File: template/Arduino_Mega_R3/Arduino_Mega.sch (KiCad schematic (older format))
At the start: 7 parts, among them P1 Digital, P2 Power, P3 Analog, P4 Analog, P5 PWM, P6 PWM, P7 Communication

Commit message: correction holes
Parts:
- added P10, P11, P12, P13, P8, P9: CONN_1, Connect:1pin, symbol CONN_1
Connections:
- no-connect marks 1 -> 7
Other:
- note added: "Holes"
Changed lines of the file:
@@
 Wire Notes Line
 	7900 6300 7900 475
+$Comp
+L CONN_1 P8
+U 1 1 551BBA20
+P 8050 650
+F 0 "P8" H 8130 650 40  0000 L CNN
+F 1 "CONN_1" H 8050 705 30  0001 C CNN
+F 2 "Connect:1pin" H 8050 650 60  0001 C CNN
+F 3 "" H 8050 650 60  0000 C CNN
+	1    8050 650
+	0    -1   -1   0
+$EndComp
+$Comp
+L CONN_1 P9
+U 1 1 551BBB85
+P 8125 650
+F 0 "P9" H 8205 650 40  0000 L CNN
+F 1 "CONN_1" H 8125 705 30  0001 C CNN
+F 2 "Connect:1pin" H 8125 650 60  0001 C CNN
+F 3 "" H 8125 650 60  0000 C CNN
+	1    8125 650
+	0    -1   -1   0
+$EndComp
+$Comp
+L CONN_1 P10
+U 1 1 551BBBAB
+P 8200 650
+F 0 "P10" H 8280 650 40  0000 L CNN
+F 1 "CONN_1" H 8200 705 30  0001 C CNN
+F 2 "Connect:1pin" H 8200 650 60  0001 C CNN
+F 3 "" H 8200 650 60  0000 C CNN
+	1    8200 650
+	0    -1   -1   0
+$EndComp
+$Comp
+L CONN_1 P11
+U 1 1 551BBBD7
+P 8275 650
+F 0 "P11" H 8355 650 40  0000 L CNN
+F 1 "CONN_1" H 8275 705 30  0001 C CNN
+F 2 "Connect:1pin" H 8275 650 60  0001 C CNN
+F 3 "" H 8275 650 60  0000 C CNN
+	1    8275 650
+	0    -1   -1   0
+$EndComp
+$Comp
+L CONN_1 P12
+U 1 1 551BBC10
+P 8350 650
+F 0 "P12" H 8430 650 40  0000 L CNN
+F 1 "CONN_1" H 8350 705 30  0001 C CNN
+F 2 "Connect:1pin" H 8350 650 60  0001 C CNN
+F 3 "" H 8350 650 60  0000 C CNN
+	1    8350 650
+	0    -1   -1   0
+$EndComp
+$Comp
+L CONN_1 P13
+U 1 1 551BBC3C
+P 8425 650
+F 0 "P13" H 8505 650 40  0000 L CNN
+F 1 "CONN_1" H 8425 705 30  0001 C CNN
+F 2 "Connect:1pin" H 8425 650 60  0001 C CNN
+F 3 "" H 8425 650 60  0000 C CNN
+	1    8425 650
+	0    -1   -1   0
+$EndComp
+NoConn ~ 8050 800
+NoConn ~ 8125 800
+NoConn ~ 8200 800
+NoConn ~ 8275 800
+NoConn ~ 8350 800
+NoConn ~ 8425 800
+Text Notes 8125 925  0    60   ~ 0
+Holes
+Wire Notes Line
+	7900 950  8575 950
+Wire Notes Line
+	8575 950  8575 475
 $EndSCHEMATC

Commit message: Correction schématics
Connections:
- net labels added: 0(Rx0), 1(Tx0), 14(Tx3), 15(Rx3), 16(Tx2), 17(Rx2), 18(Tx1), 19(Rx1)
- net labels removed: 0(Rx), 1(Tx), 14(Tx), 15(Rx), 16(Tx), 17(Rx), 18(Tx), 19(Rx)
- wire segments 96 -> 98
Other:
- moved on the sheet: P10, P11, P12, P13, P2, P3, P4, P5, P6, P7, P8, P9

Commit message: corrections
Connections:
- net labels removed: NC
- wire segments 98 -> 97
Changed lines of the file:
@@
 	-1   0    0    -1
 $EndComp
-NoConn ~ 8425 1425
-Text Label 8450 1425 0    60   ~ 0
-NC
+NoConn ~ 9200 1425
 Text Label 9125 1250 1    60   ~ 0
 IOREF
@@
 Connection ~ 9125 2025
 Wire Wire Line
-	9200 1425 8425 1425
-Wire Wire Line
 	9200 1625 8425 1625

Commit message: add footprint Uno and Mega
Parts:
- P10, P11, P12, P13, P8, P9: footprint Connect:1pin -> Socket_Arduino_Mega:Arduino_1pin
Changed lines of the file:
@@
 F 0 "P8" H 10805 700 40  0000 L CNN
 F 1 "CONN_1" H 10725 755 30  0001 C CNN
-F 2 "Connect:1pin" H 10725 700 60  0001 C CNN
+F 2 "Socket_Arduino_Mega:Arduino_1pin" H 10725 700 60  0001 C CNN
 F 3 "" H 10725 700 60  0000 C CNN
 	1    10725 700
@@
 F 0 "P9" H 10880 700 40  0000 L CNN
 F 1 "CONN_1" H 10800 755 30  0001 C CNN
-F 2 "Connect:1pin" H 10800 700 60  0001 C CNN
+F 2 "Socket_Arduino_Mega:Arduino_1pin" H 10800 700 60  0001 C CNN
 F 3 "" H 10800 700 60  0000 C CNN
 	1    10800 700
@@
 F 0 "P10" H 10955 700 40  0000 L CNN
 F 1 "CONN_1" H 10875 755 30  0001 C CNN
-F 2 "Connect:1pin" H 10875 700 60  0001 C CNN
+F 2 "Socket_Arduino_Mega:Arduino_1pin" H 10875 700 60  0001 C CNN
 F 3 "" H 10875 700 60  0000 C CNN
 	1    10875 700
@@
 F 0 "P11" H 11030 700 40  0000 L CNN
 F 1 "CONN_1" H 10950 755 30  0001 C CNN
-F 2 "Connect:1pin" H 10950 700 60  0001 C CNN
+F 2 "Socket_Arduino_Mega:Arduino_1pin" H 10950 700 60  0001 C CNN
 F 3 "" H 10950 700 60  0000 C CNN
 	1    10950 700
@@
 F 0 "P12" H 11105 700 40  0000 L CNN
 F 1 "CONN_1" H 11025 755 30  0001 C CNN
-F 2 "Connect:1pin" H 11025 700 60  0001 C CNN
+F 2 "Socket_Arduino_Mega:Arduino_1pin" H 11025 700 60  0001 C CNN
 F 3 "" H 11025 700 60  0000 C CNN
 	1    11025 700
@@
 F 0 "P13" H 11180 700 40  0000 L CNN
 F 1 "CONN_1" H 11100 755 30  0001 C CNN
-F 2 "Connect:1pin" H 11100 700 60  0001 C CNN
+F 2 "Socket_Arduino_Mega:Arduino_1pin" H 11100 700 60  0001 C CNN
 F 3 "" H 11100 700 60  0000 C CNN
 	1    11100 700

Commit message: rebuilt shematic and fix librairie
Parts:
- removed P1: Digital, Socket_Arduino_Mega:Socket_Strip_Arduino_2x18, symbol CONN_18X2
- removed P10, P11, P12, P13, P8, P9: CONN_1, Socket_Arduino_Mega:Arduino_1pin, symbol CONN_1
- removed P2: Power, Socket_Arduino_Mega:Socket_Strip_Arduino_1x08, symbol CONN_8
- removed P3, P4: Analog, Socket_Arduino_Mega:Socket_Strip_Arduino_1x08, symbol CONN_8
- removed P5: PWM, Socket_Arduino_Mega:Socket_Strip_Arduino_1x10, symbol CONN_10
- removed P6: PWM, Socket_Arduino_Mega:Socket_Strip_Arduino_1x08, symbol CONN_8
- removed P7: Communication, Socket_Arduino_Mega:Socket_Strip_Arduino_1x08, symbol CONN_8
- added P1: Digital, Socket_Arduino_Mega:Socket_Strip_Arduino_2x18, symbol CONN_02X18
- added P10, P11, P12, P13, P8, P9: CONN_01X01, Socket_Arduino_Mega:Arduino_1pin, symbol CONN_01X01
- added P2: Power, Socket_Arduino_Mega:Socket_Strip_Arduino_1x08, symbol CONN_01X08
- added P3, P4: Analog, Socket_Arduino_Mega:Socket_Strip_Arduino_1x08, symbol CONN_01X08
- added P5: PWM, Socket_Arduino_Mega:Socket_Strip_Arduino_1x10, symbol CONN_01X10
- added P6: PWM, Socket_Arduino_Mega:Socket_Strip_Arduino_1x08, symbol CONN_01X08
- added P7: Communication, Socket_Arduino_Mega:Socket_Strip_Arduino_1x08, symbol CONN_01X08
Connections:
- wire segments 97 -> 93
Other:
- note added: "1"

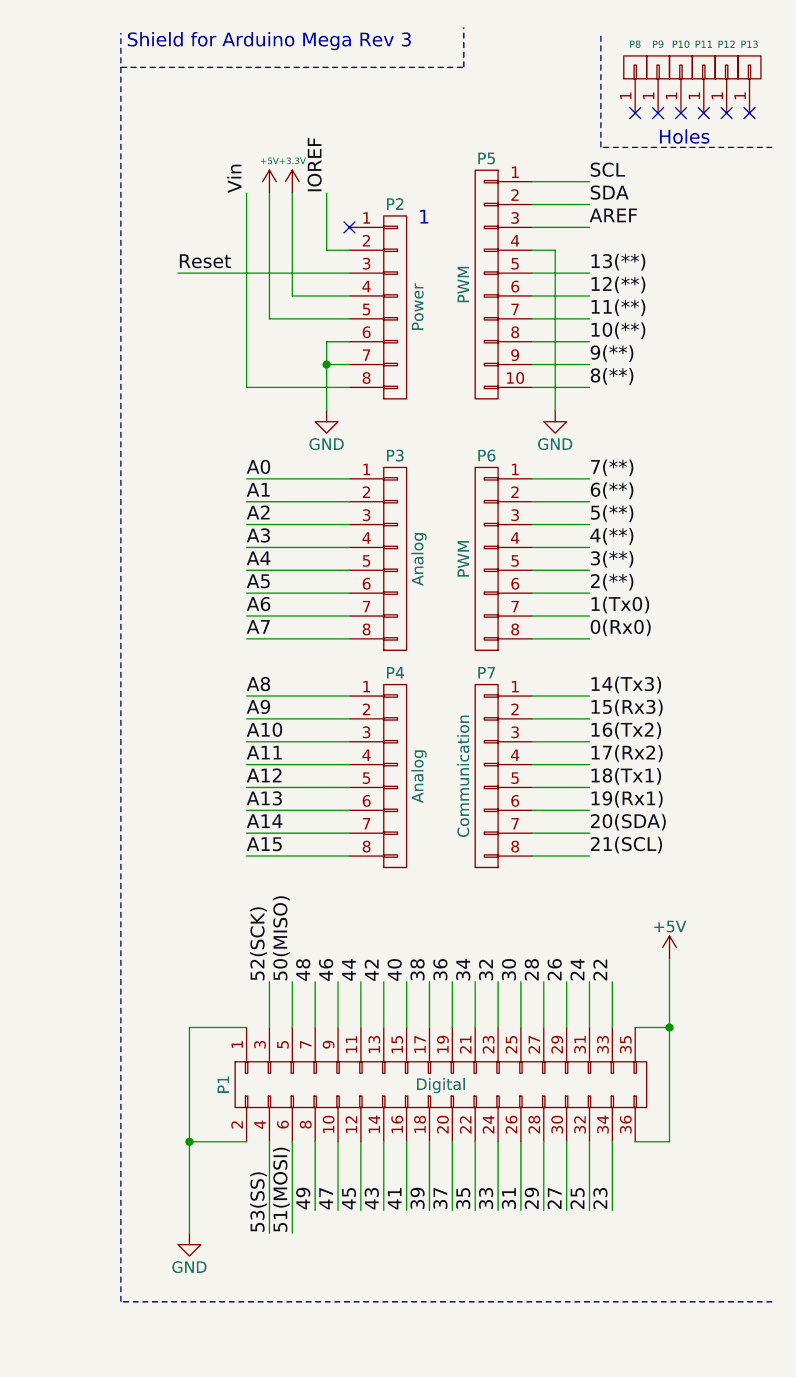
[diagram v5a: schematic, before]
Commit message: fix template
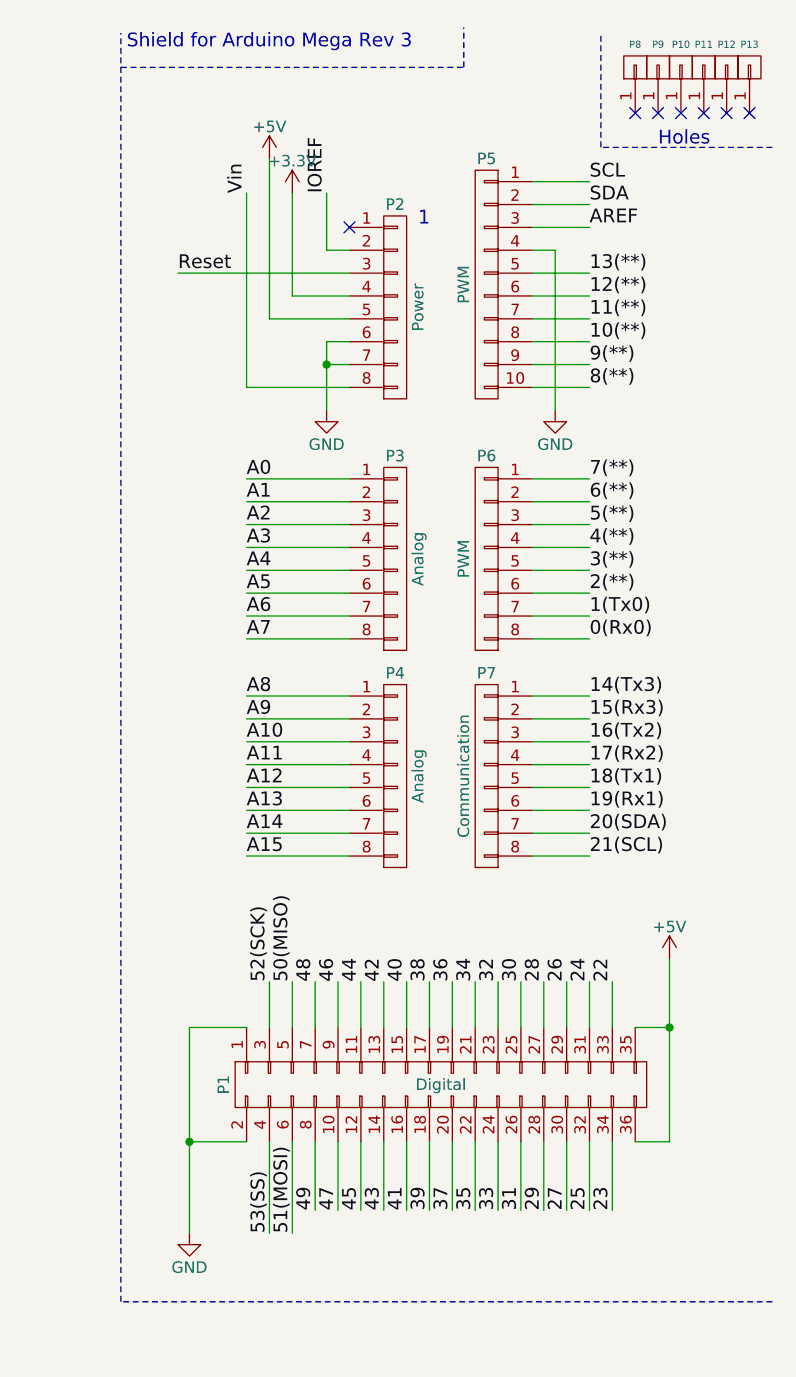
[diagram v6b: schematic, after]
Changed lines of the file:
@@
 P 9100 1200
 F 0 "#PWR01" H 9100 1050 50  0001 C CNN
-F 1 "+3.3V" H 9100 1340 28  0000 C CNN
+F 1 "+3.3V" H 9100 1340 50  0000 C CNN
 F 2 "" H 9100 1200 50  0000 C CNN
 F 3 "" H 9100 1200 50  0000 C CNN
@@
 L +5V #PWR02
 U 1 1 56D71D10
-P 9000 1200
-F 0 "#PWR02" H 9000 1050 50  0001 C CNN
-F 1 "+5V" H 9000 1340 28  0000 C CNN
-F 2 "" H 9000 1200 50  0000 C CNN
-F 3 "" H 9000 1200 50  0000 C CNN
-	1    9000 1200
+P 9000 1050
+F 0 "#PWR02" H 9000 900 50  0001 C CNN
+F 1 "+5V" H 9000 1190 50  0000 C CNN
+F 2 "" H 9000 1050 50  0000 C CNN
+F 3 "" H 9000 1050 50  0000 C CNN
+	1    9000 1050
 	1    0    0    -1
 $EndComp
@@
 	9100 1650 9350 1650
 Wire Wire Line
-	9000 1200 9000 1750
+	9000 1050 9000 1750
 Wire Wire Line
 	9000 1750 9350 1750
@@
 	9350 1850 9250 1850
 Wire Wire Line
-	9250 1850 9250 2150
+	9250 1850 9250 1950
+Wire Wire Line
+	9250 1950 9250 2150
 Wire Wire Line
 	9350 1950 9250 1950
@@
 Connection ~ 10750 4850
 Wire Wire Line
-	10750 4550 10750 5350
-Wire Wire Line
-	8650 4850 8650 5750
+	10750 4550 10750 4850
+Wire Wire Line
+	10750 4850 10750 5350
+Wire Wire Line
+	8650 4850 8650 5350
+Wire Wire Line
+	8650 5350 8650 5750
 Wire Notes Line
 	11200 6050 8350 6050
